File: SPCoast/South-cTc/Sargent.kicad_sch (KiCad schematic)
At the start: 9 parts, among them U33 0x2C

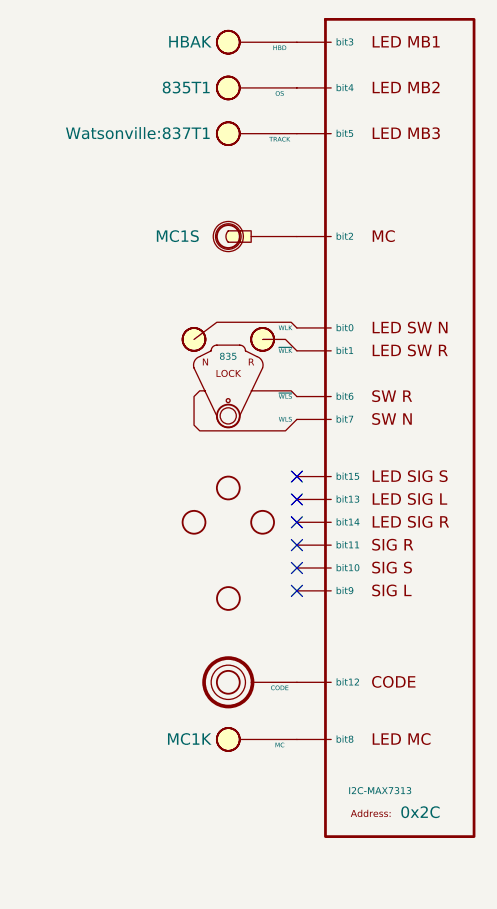
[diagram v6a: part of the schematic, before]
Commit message: chore(kicad): desk sheets to Driver-I2C-MAX7313 and the PanelLock Kind (InterlockingPlant owner review)
- 14 desk expanders: lib_id RailroadPanel:PanelColumn-MAX7313 -> Driver-I2C-MAX7313, embedded
  definition refreshed (pins A1..B8, same numbers and positions).
- 8 PanelLock instances: Kind LOCK_LEVER -> LOCK_LEVER_2LAMP_2CONTACT (7 desk, 1 Sargent sandbox).

Verified:
- verify_symbol_diff.py: only those lib_id and Kind changes.
- South-cTc 341 nets, Sargent 61; desk compile 75/137/14 with bindings identical to e2c1093.

Co-Authored-By: Claude Opus 5.5 <noreply@anthropic.com>
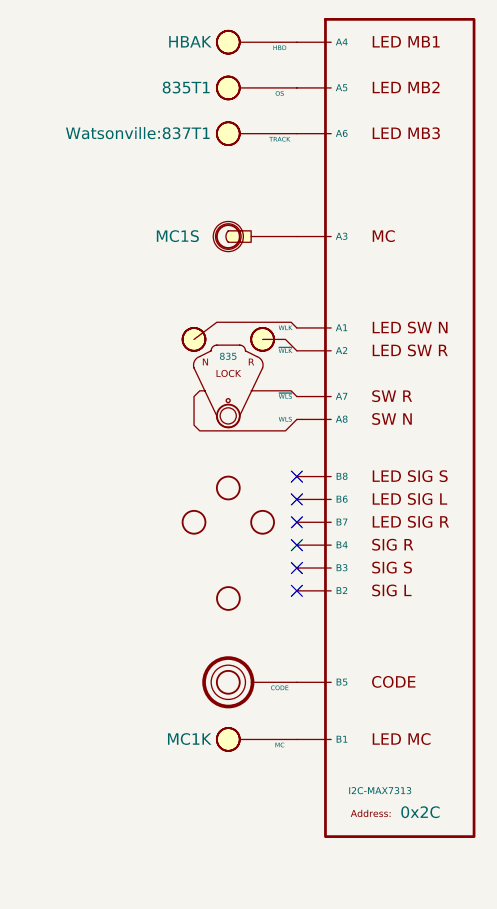
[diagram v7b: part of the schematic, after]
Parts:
- LKL13: Kind LOCK_LEVER -> LOCK_LEVER_2LAMP_2CONTACT
- U33: symbol RailroadPanel:PanelColumn-MAX7313 -> RailroadPanel:Driver-I2C-MAX7313
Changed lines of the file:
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@@
 	)
 	(symbol
-		(lib_id "RailroadPanel:PanelColumn-MAX7313")
+		(lib_id "RailroadPanel:Driver-I2C-MAX7313")
 		(at 99.06 72.39 0)
 		(unit 1)
@@
 			)
 		)
-		(property "Kind" "LOCK_LEVER"
+		(property "Kind" "LOCK_LEVER_2LAMP_2CONTACT"
 			(at 80.645 73.025 0)
 			(hide yes)
